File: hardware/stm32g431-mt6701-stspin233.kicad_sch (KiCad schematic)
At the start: 16 parts, among them J101 I2C, J102 UART, J103 CANBUS_IN, J104 CANBUS_OUT, J106 CAN TERMINATION, J107 EXT_PWR, J109 MOT_FPC, J110 MOT_FPC2, U101 SN65HVD230

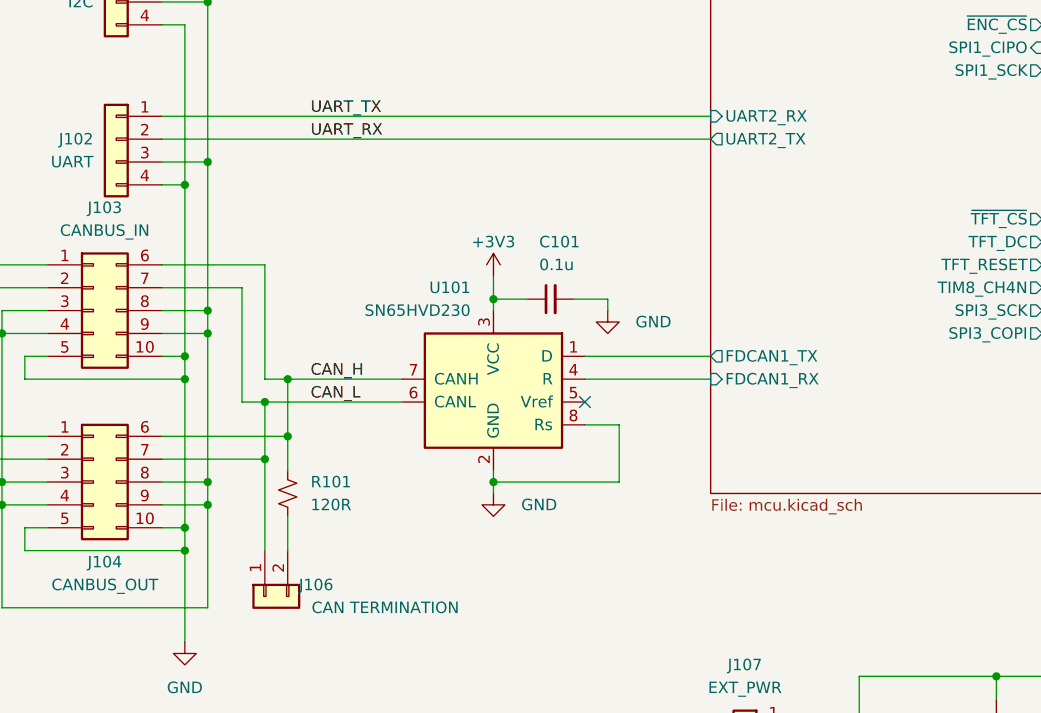
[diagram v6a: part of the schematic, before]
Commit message: get USB detection working
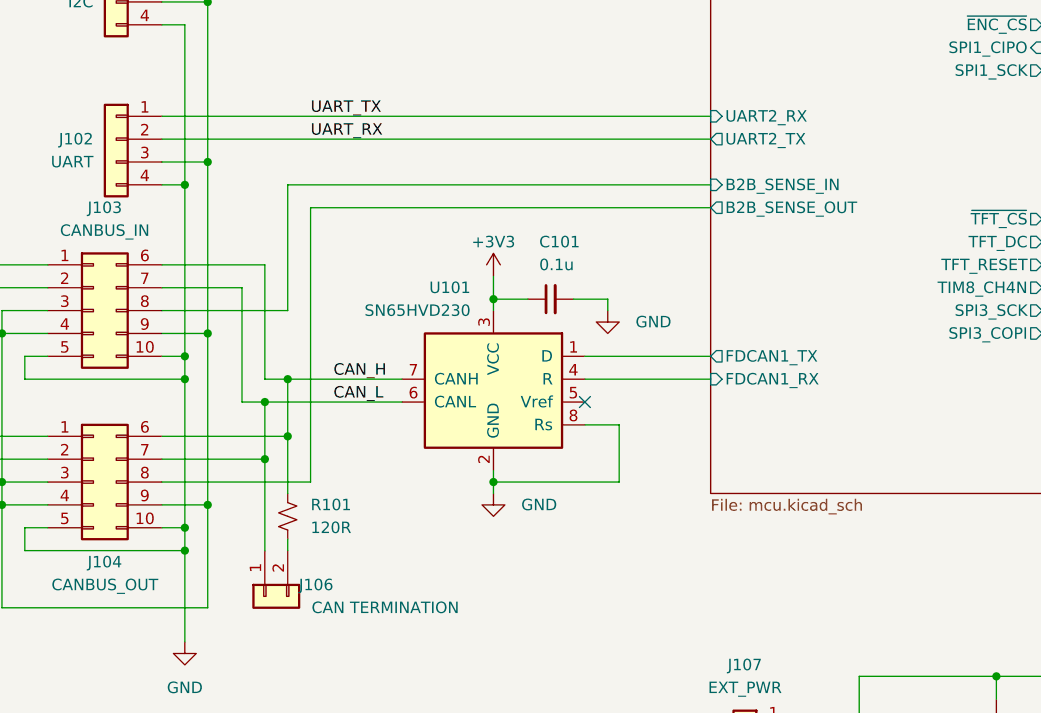
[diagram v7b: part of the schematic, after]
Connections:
- net Vmot: no longer J103.8 (Pin_8), J104.8 (Pin_8)
- new net mcu/B2B_SENSE_IN: J103.8 (Pin_8)
- new net mcu/B2B_SENSE_OUT: J104.8 (Pin_8)
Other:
- sheet mcu ports: added B2B_SENSE_IN, B2B_SENSE_OUT; removed none
- moved on the sheet: R101
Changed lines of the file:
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@@
   (junction (at 26.67 116.84) (diameter 0) (color 0 0 0 0)
   )
-  (junction (at 49.53 97.79) (diameter 0) (color 0 0 0 0)
-  )
   (junction (at 49.53 63.5) (diameter 0) (color 0 0 0 0)
   )
@@
   )
   (junction (at 46.99 124.46) (diameter 0) (color 0 0 0 0)
-  )
-  (junction (at 49.53 116.84) (diameter 0) (color 0 0 0 0)
   )
   (junction (at 81.28 116.84) (diameter 0) (color 0 0 0 0)
@@
     (stroke (width 0) (type default))
   )
-  (wire (pts (xy 49.53 116.84) (xy 49.53 119.38))
+  (wire (pts (xy 49.53 100.33) (xy 49.53 119.38))
     (stroke (width 0) (type default))
   )
@@
     (stroke (width 0) (type default))
   )
+  (wire (pts (xy 44.45 116.84) (xy 60.96 116.84))
+    (stroke (width 0) (type default))
+  )
   (wire (pts (xy 53.34 95.25) (xy 53.34 107.95))
     (stroke (width 0) (type default))
@@
     (stroke (width 0) (type default))
   )
+  (wire (pts (xy 60.96 86.36) (xy 105.41 86.36))
+    (stroke (width 0) (type default))
+  )
   (wire (pts (xy 142.24 71.12) (xy 160.02 71.12))
     (stroke (width 0) (type default))
@@
     (stroke (width 0) (type default))
   )
+  (wire (pts (xy 60.96 116.84) (xy 60.96 86.36))
+    (stroke (width 0) (type default))
+  )
   (wire (pts (xy 26.67 97.79) (xy 31.75 97.79))
     (stroke (width 0) (type default))
@@
     (stroke (width 0) (type default))
   )
-  (wire (pts (xy 49.53 100.33) (xy 49.53 116.84))
-    (stroke (width 0) (type default))
-  )
-  (wire (pts (xy 44.45 116.84) (xy 49.53 116.84))
-    (stroke (width 0) (type default))
-  )
   (wire (pts (xy 200.66 148.59) (xy 209.55 148.59))
     (stroke (width 0) (type default))
@@
     (stroke (width 0) (type default))
   )
-  (wire (pts (xy 44.45 97.79) (xy 49.53 97.79))
-    (stroke (width 0) (type default))
-  )
   (wire (pts (xy 17.78 111.76) (xy 31.75 111.76))
     (stroke (width 0) (type default))
@@
     (stroke (width 0) (type default))
   )
+  (wire (pts (xy 44.45 97.79) (xy 58.42 97.79))
+    (stroke (width 0) (type default))
+  )
   (wire (pts (xy 157.48 113.03) (xy 181.61 113.03))
     (stroke (width 0) (type default))
@@
     (stroke (width 0) (type default))
   )
-  (wire (pts (xy 58.42 120.65) (xy 58.42 124.46))
+  (wire (pts (xy 58.42 123.19) (xy 58.42 124.46))
     (stroke (width 0) (type default))
   )
@@
     (stroke (width 0) (type default))
   )
+  (wire (pts (xy 58.42 97.79) (xy 58.42 83.82))
+    (stroke (width 0) (type default))
+  )
   (wire (pts (xy 95.25 116.84) (xy 81.28 116.84))
     (stroke (width 0) (type default))
   )
-  (wire (pts (xy 49.53 81.28) (xy 49.53 97.79))
+  (wire (pts (xy 49.53 81.28) (xy 49.53 100.33))
     (stroke (width 0) (type default))
   )
@@
     (stroke (width 0) (type default))
   )
-  (wire (pts (xy 49.53 97.79) (xy 49.53 100.33))
-    (stroke (width 0) (type default))
-  )
   (wire (pts (xy 55.88 105.41) (xy 58.42 105.41))
     (stroke (width 0) (type default))
   )
-  (wire (pts (xy 58.42 111.76) (xy 58.42 115.57))
+  (wire (pts (xy 58.42 111.76) (xy 58.42 118.11))
     (stroke (width 0) (type default))
   )
@@
     (stroke (width 0) (type default))
   )
+  (wire (pts (xy 58.42 105.41) (xy 71.12 105.41))
+    (stroke (width 0) (type default))
+  )
   (wire (pts (xy 91.44 105.41) (xy 105.41 105.41))
     (stroke (width 0) (type default))
@@
     (stroke (width 0) (type default))
   )
-  (wire (pts (xy 58.42 105.41) (xy 71.12 105.41))
-    (stroke (width 0) (type default))
-  )
   (wire (pts (xy 137.16 148.59) (xy 137.16 151.13))
     (stroke (width 0) (type default))
@@
   )
   (wire (pts (xy 217.17 40.64) (xy 217.17 52.07))
+    (stroke (width 0) (type default))
+  )
+  (wire (pts (xy 58.42 83.82) (xy 105.41 83.82))
     (stroke (width 0) (type default))
   )
@@
     (effects (font (size 1.27 1.27)) (justify left bottom))
   )
-  (label "CAN_H" (at 60.96 105.41 0) (fields_autoplaced)
+  (label "CAN_H" (at 63.5 105.41 0) (fields_autoplaced)
     (effects (font (size 1.27 1.27)) (justify left bottom))
   )
-  (label "CAN_L" (at 60.96 107.95 0) (fields_autoplaced)
+  (label "CAN_L" (at 63.5 107.95 0) (fields_autoplaced)
     (effects (font (size 1.27 1.27)) (justify left bottom))
   )
@@
     (effects (font (size 1.27 1.27)) (justify left bottom))
   )
-  (symbol (lib_id "Device:R_Small_US") (at 58.42 118.11 180) (unit 1)
+  (symbol (lib_id "Device:R_Small_US") (at 58.42 120.65 180) (unit 1)
     (in_bom yes) (on_board yes) (dnp no)
-    (property "Reference" "R101" (at 60.96 116.84 0)
-      (effects (font (size 1.27 1.27)) (justify right))
-    )
-    (property "Value" "120R" (at 60.96 119.38 0)
-      (effects (font (size 1.27 1.27)) (justify right))
-    )
-    (property "Footprint" "Resistor_SMD:R_0402_1005Metric" (at 58.42 118.11 0)
-      (effects (font (size 1.27 1.27)) hide)
-    )
-    (property "Datasheet" "~" (at 58.42 118.11 0)
+    (property "Reference" "R101" (at 60.96 119.38 0)
+      (effects (font (size 1.27 1.27)) (justify right))
+    )
+    (property "Value" "120R" (at 60.96 121.92 0)
+      (effects (font (size 1.27 1.27)) (justify right))
+    )
+    (property "Footprint" "Resistor_SMD:R_0402_1005Metric" (at 58.42 120.65 0)
+      (effects (font (size 1.27 1.27)) hide)
+    )
+    (property "Datasheet" "~" (at 58.42 120.65 0)
       (effects (font (size 1.27 1.27)) hide)
     )
@@
       (effects (font (size 1.27 1.27)) (justify right))
     )
-    (instances
+    (pin "B2B_SENSE_IN" input (at 105.41 83.82 180)
+      (effects (font (size 1.27 1.27)) (justify left))
+    )
+    (pin "B2B_SENSE_OUT" output (at 105.41 86.36 180)
+      (effects (font (size 1.27 1.27)) (justify left))
+    )
+    (instances
